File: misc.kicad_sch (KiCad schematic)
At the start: 50 parts, among them J1 Serial 1, J14 Paddles, J15 Conn_02x07_Row_Letter_Last, J17 Conn_02x04_Row_Letter_Last, J18 Conn_02x04_Top_Bottom, J19 I2C, J21 Serial 2, J22 Rotary Encoder, J24 LCD, J3 Serial 2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

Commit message: Changed many capacitor part numbers.
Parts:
- C1, C2, C3, C4, C5, C6: footprint Capacitor_SMD:C_1206_3216Metric -> Capacitor_SMD:C_0603_1608Metric; JLCPCB_PN C2169061 -> C57112
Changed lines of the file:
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@@
       (effects (font (size 1.27 1.27)) (justify left))
     )
-    (property "Footprint" "Capacitor_SMD:C_1206_3216Metric" (at 237.7948 101.6 0)
+    (property "Footprint" "Capacitor_SMD:C_0603_1608Metric" (at 237.7948 101.6 0)
       (effects (font (size 1.27 1.27)) hide)
     )
@@
       (effects (font (size 1.27 1.27)) hide)
     )
-    (property "JLCPCB_PN" "C2169061" (at 238.76 97.79 0)
+    (property "JLCPCB_PN" "C57112" (at 238.76 97.79 0)
       (effects (font (size 1.27 1.27)) hide)
     )
@@
       (effects (font (size 1.27 1.27)) (justify left))
     )
-    (property "Footprint" "Capacitor_SMD:C_1206_3216Metric" (at 35.8648 50.8 0)
+    (property "Footprint" "Capacitor_SMD:C_0603_1608Metric" (at 35.8648 50.8 0)
       (effects (font (size 1.27 1.27)) hide)
     )
@@
       (effects (font (size 1.27 1.27)) hide)
     )
-    (property "JLCPCB_PN" "C2169061" (at 36.83 46.99 0)
+    (property "JLCPCB_PN" "C57112" (at 36.83 46.99 0)
       (effects (font (size 1.27 1.27)) hide)
     )
@@
       (effects (font (size 1.27 1.27)) (justify left))
     )
-    (property "Footprint" "Capacitor_SMD:C_1206_3216Metric" (at 46.0248 50.8 0)
+    (property "Footprint" "Capacitor_SMD:C_0603_1608Metric" (at 46.0248 50.8 0)
       (effects (font (size 1.27 1.27)) hide)
     )
@@
       (effects (font (size 1.27 1.27)) hide)
     )
-    (property "JLCPCB_PN" "C2169061" (at 46.99 46.99 0)
+    (property "JLCPCB_PN" "C57112" (at 46.99 46.99 0)
       (effects (font (size 1.27 1.27)) hide)
     )
@@
       (effects (font (size 1.27 1.27)) (justify left))
     )
-    (property "Footprint" "Capacitor_SMD:C_1206_3216Metric" (at 217.4748 60.96 0)
+    (property "Footprint" "Capacitor_SMD:C_0603_1608Metric" (at 217.4748 60.96 0)
       (effects (font (size 1.27 1.27)) hide)
     )
@@
       (effects (font (size 1.27 1.27)) hide)
     )
-    (property "JLCPCB_PN" "C2169061" (at 218.44 57.15 0)
+    (property "JLCPCB_PN" "C57112" (at 218.44 57.15 0)
       (effects (font (size 1.27 1.27)) hide)
     )
@@
       (effects (font (size 1.27 1.27)) (justify left))
     )
-    (property "Footprint" "Capacitor_SMD:C_1206_3216Metric" (at 237.7948 72.39 0)
+    (property "Footprint" "Capacitor_SMD:C_0603_1608Metric" (at 237.7948 72.39 0)
       (effects (font (size 1.27 1.27)) hide)
     )
@@
       (effects (font (size 1.27 1.27)) hide)
     )
-    (property "JLCPCB_PN" "C2169061" (at 238.76 68.58 0)
+    (property "JLCPCB_PN" "C57112" (at 238.76 68.58 0)
       (effects (font (size 1.27 1.27)) hide)
     )
@@
       (effects (font (size 1.27 1.27)) (justify left))
     )
-    (property "Footprint" "Capacitor_SMD:C_1206_3216Metric" (at 217.4748 90.17 0)
+    (property "Footprint" "Capacitor_SMD:C_0603_1608Metric" (at 217.4748 90.17 0)
       (effects (font (size 1.27 1.27)) hide)
     )
@@
       (effects (font (size 1.27 1.27)) hide)
     )
-    (property "JLCPCB_PN" "C2169061" (at 218.44 86.36 0)
-      (effects (font (size 1.27 1.27)) hide)
-    )
+    (property "JLCPCB_PN" "C57112" (at 218.44 86.36 0)
+      (effects (font (size 1.27 1.27)) hide)
+    )

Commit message: Fixed variable resistor parts (forgot to save before committing).
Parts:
- RV5: footprint Resistor_SMD:R_0805_2012Metric -> Potentiometer_SMD:Potentiometer_Bourns_3314J_Vertical; JLCPCB_PN C4340265 -> C124621
- RV6: footprint Resistor_SMD:R_0805_2012Metric -> Potentiometer_SMD:Potentiometer_Bourns_3314J_Vertical; JLCPCB_PN C2828857 -> C123873
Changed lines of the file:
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@@
       (effects (font (size 1.27 1.27)) (justify right))
     )
-    (property "Footprint" "Resistor_SMD:R_0805_2012Metric" (at 203.2 135.89 0)
+    (property "Footprint" "Potentiometer_SMD:Potentiometer_Bourns_3314J_Vertical" (at 203.2 135.89 0)
       (effects (font (size 1.27 1.27)) hide)
     )
@@
       (effects (font (size 1.27 1.27)) hide)
     )
-    (property "JLCPCB_PN" "C4340265" (at 203.2 135.89 0)
+    (property "JLCPCB_PN" "C124621" (at 203.2 135.89 0)
       (effects (font (size 1.27 1.27)) hide)
     )
@@
       (effects (font (size 1.27 1.27)) (justify right))
     )
-    (property "Footprint" "Resistor_SMD:R_0805_2012Metric" (at 247.65 133.35 0)
+    (property "Footprint" "Potentiometer_SMD:Potentiometer_Bourns_3314J_Vertical" (at 247.65 133.35 0)
       (effects (font (size 1.27 1.27)) hide)
     )
@@
       (effects (font (size 1.27 1.27)) hide)
     )
-    (property "JLCPCB_PN" "C2828857" (at 247.65 133.35 0)
-      (effects (font (size 1.27 1.27)) hide)
-    )
+    (property "JLCPCB_PN" "C123873" (at 247.65 133.35 0)
+      (effects (font (size 1.27 1.27)) hide)
+    )

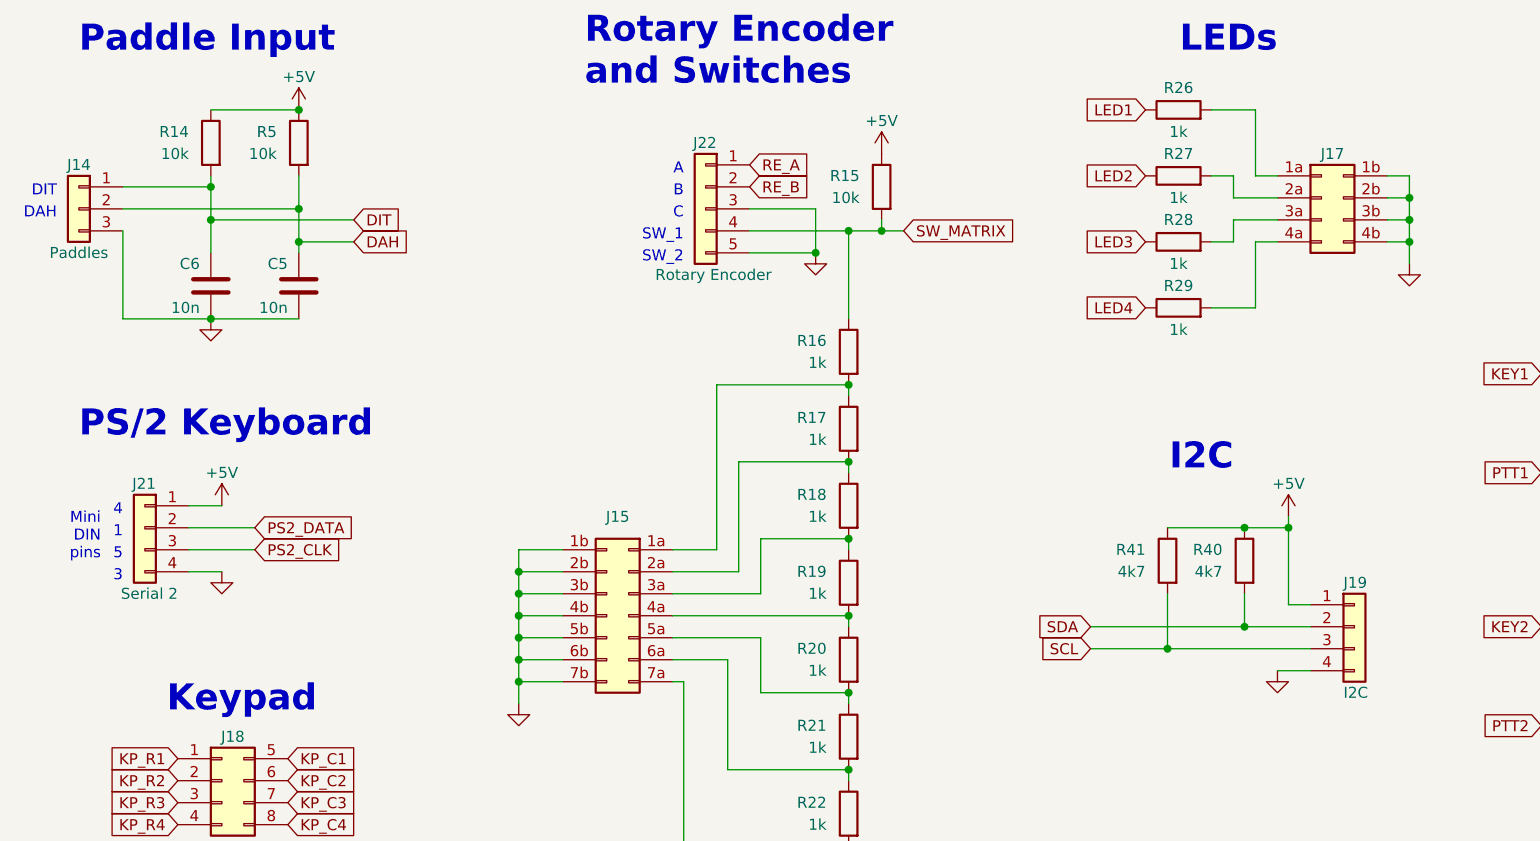
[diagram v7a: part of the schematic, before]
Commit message: First attempt at locating parts on PCB. Also, many changes to footprints.
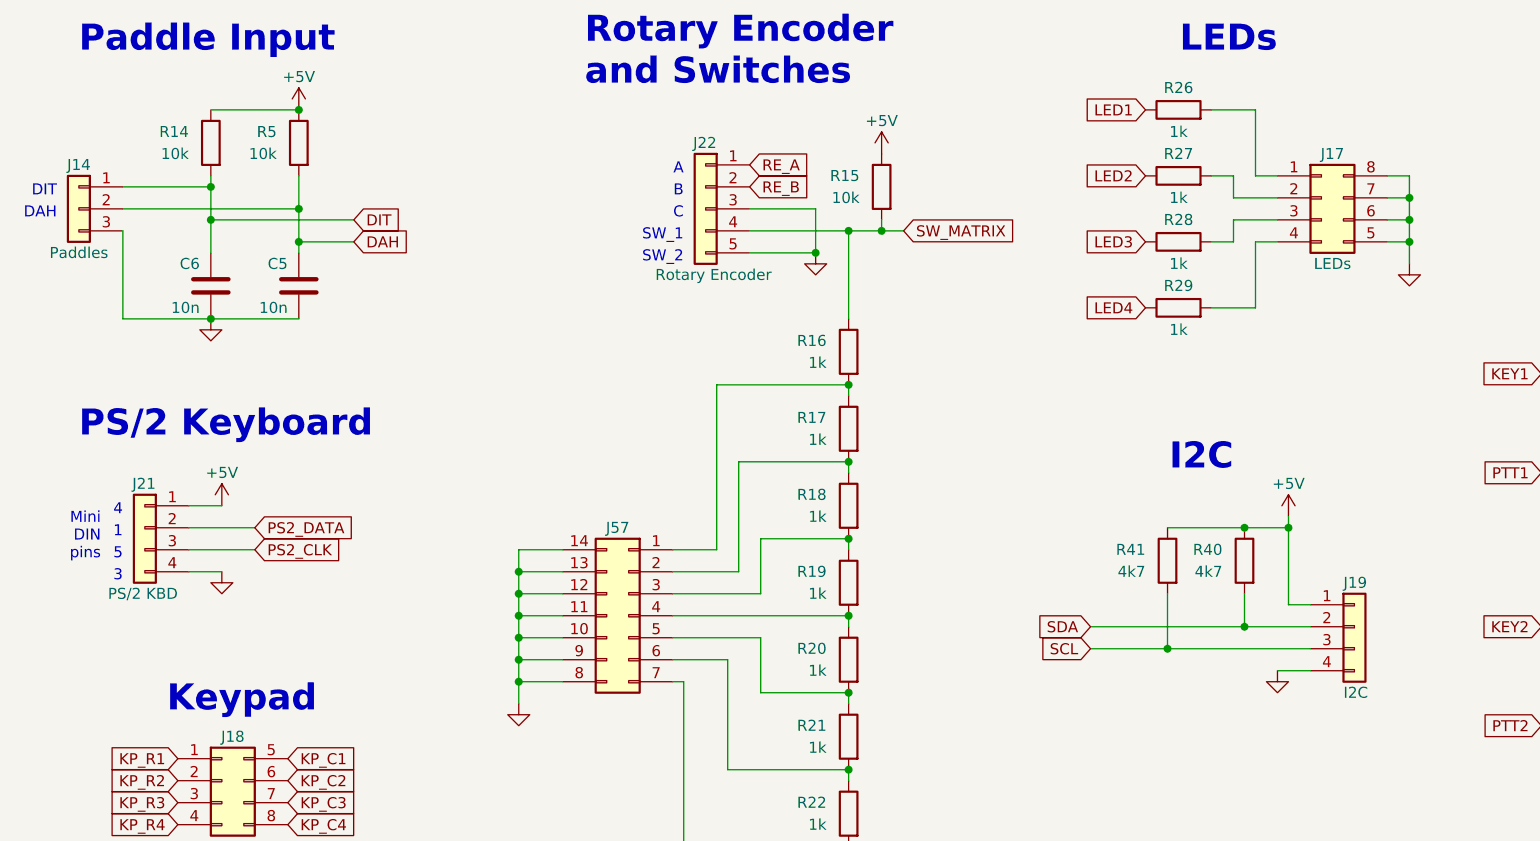
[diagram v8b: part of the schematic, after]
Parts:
- removed J15: Conn_02x07_Row_Letter_Last, Connector_PinHeader_2.54mm:PinHeader_2x07_P2.54mm_Vertical, symbol Connector_Generic:Conn_02x07_Row_Letter_Last
- removed J17: Conn_02x04_Row_Letter_Last, Connector_PinHeader_2.54mm:PinHeader_2x04_P2.54mm_Vertical, symbol Connector_Generic:Conn_02x04_Row_Letter_Last
- added J17: LEDs, Connector_PinHeader_2.54mm:PinHeader_2x04_P2.54mm_Vertical, symbol Connector_Generic:Conn_02x04_Counter_Clockwise
- added J57: Conn_02x07_Counter_Clockwise, Connector_PinHeader_2.54mm:PinHeader_2x07_P2.54mm_Vertical, symbol Connector_Generic:Conn_02x07_Counter_Clockwise
- J19: footprint Connector_PinHeader_2.54mm:PinHeader_2x04_P2.54mm_Vertical -> Connector_PinHeader_2.54mm:PinHeader_1x04_P2.54mm_Vertical
- J21: value Serial 2 -> PS/2 KBD
- PTT-JP2, PTT-JP3: footprint Connector_PinHeader_2.54mm:PinHeader_1x05_P2.54mm_Vertical -> Jumper:SolderJumper-2_P1.3mm_Open_TrianglePad1.0x1.5mm
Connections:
- net GND: now also J17.5 (Pin_5), J17.6 (Pin_6), J17.7 (Pin_7), J17.8 (Pin_8), J57.10 (Pin_10), J57.11 (Pin_11), J57.12 (Pin_12), J57.13 (Pin_13), J57.14 (Pin_14), J57.8 (Pin_8), J57.9 (Pin_9)
- net at R16.2, R17.1: now also J57.1 (Pin_1)
- net at R17.2, R18.1: now also J57.2 (Pin_2)
- net at R19.2, R20.1: now also J57.4 (Pin_4)
- net at R20.2, R21.1: now also J57.5 (Pin_5)
- net at R18.2, R19.1: now also J57.3 (Pin_3)
- net at R21.2, R22.1: now also J57.6 (Pin_6)
- net at R22.2: now also J57.7 (Pin_7)
- net at R28.2: now also J17.3 (Pin_3)
- net at R29.2: now also J17.4 (Pin_4)
- net at R26.2: now also J17.1 (Pin_1)
- net at R27.2: now also J17.2 (Pin_2)
